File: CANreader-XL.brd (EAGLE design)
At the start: 66.7 x 61 mm, 73 parts, among them IC2 TJA1055T, IC3 BD9G101G, IC4 LM1117IMPX-3.3, IC5 STM32F107VBT, Q1 16MHz, U1 HC_05, U2 MCP2551, X1 MINI-USB, X2 SWD, X3 GPIO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

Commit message: Mount hole
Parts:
- moved LED1 0.51 mm to (3.17, 51.3), turned to 90 degrees
- moved LED3 0.25 mm to (3.17, 56.1)
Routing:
- net +3V3: track 361.5 -> 359.8 mm
- net GND: track 877.0 -> 875.7 mm
- net USB_VBUS: track 34.0 -> 35.2 mm
- net USB_D-: track 32.0 -> 33.2 mm
- net N$18: track 24.6 -> 23.4 mm
- net USB_D+: track 31.1 -> 32.1 mm
- net N$14: track 12.8 -> 13.4 mm

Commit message: Board name & version
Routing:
- net +3V3: track 359.8 -> 355.4 mm
- net PD7: track 55.6 -> 54.6 mm
- net PB10: track 16.1 -> 15.3 mm
- net PD4: track 61.4 -> 60.6 mm
- net PD3: track 73.3 -> 72.6 mm
- net RMII_MDC: track 48.1 -> 47.6 mm
- net RMII_REF_CLK: track 42.1 -> 41.6 mm
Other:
- board text added: "CANreader-XL"
- board text added: "https://github.com/autowp/CANreader-XL"
- board text added: "v0.1"

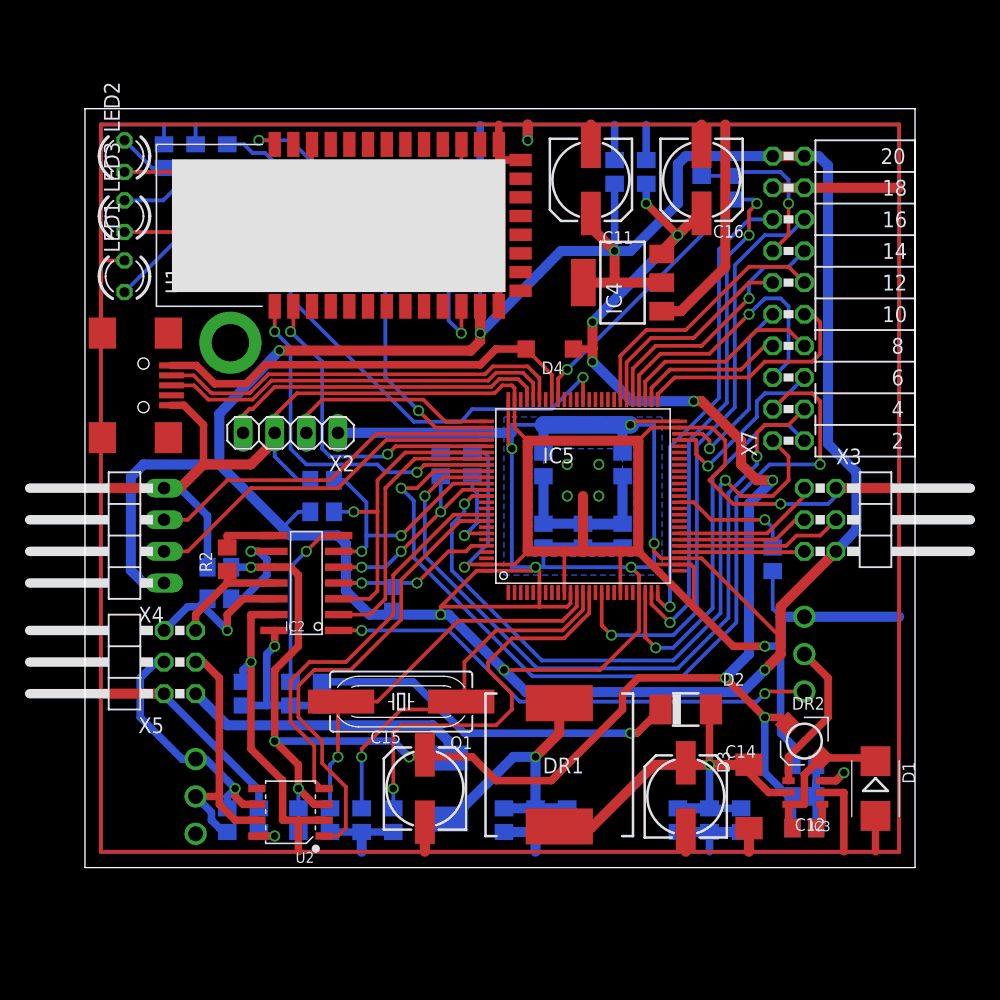
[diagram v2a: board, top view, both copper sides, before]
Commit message: Silk layers
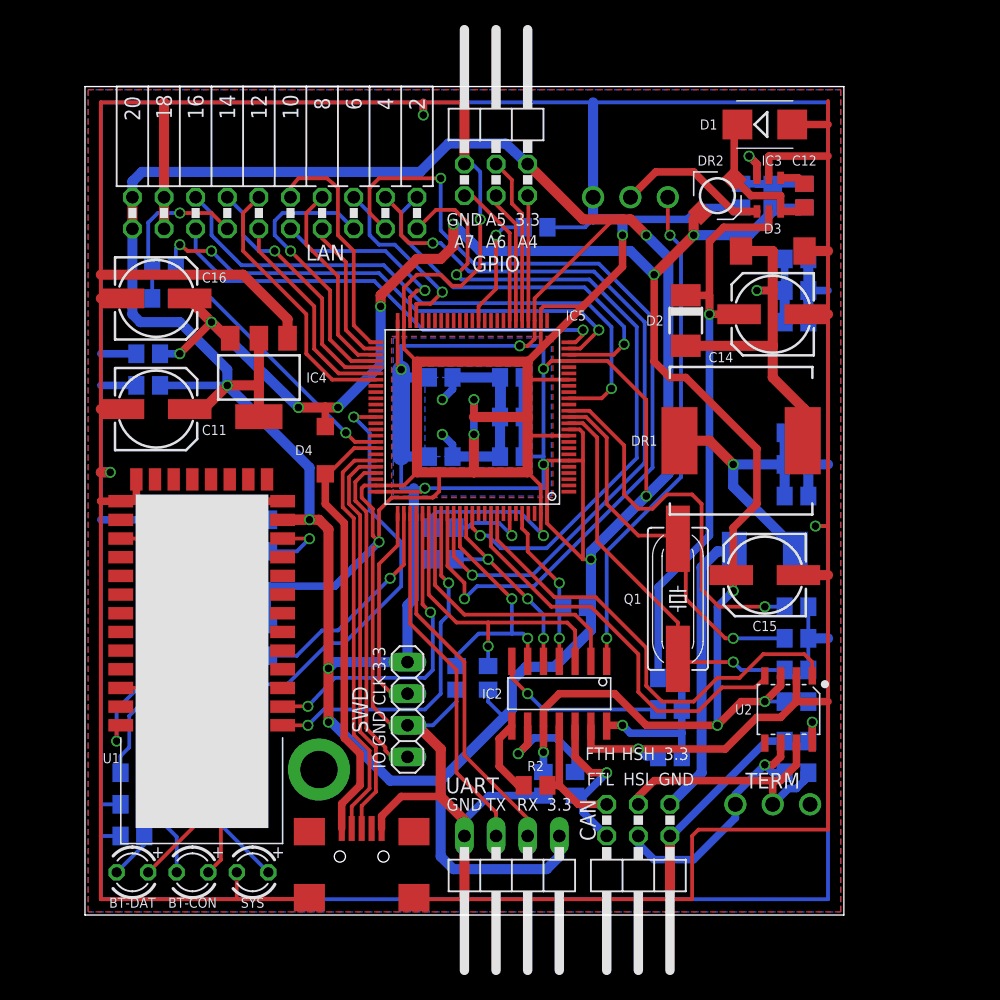
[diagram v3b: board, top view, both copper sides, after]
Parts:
- LED1: value USER -> SYS
- LED2: value HC-DATA -> BT-DAT
- LED3: value HC-CONN -> BT-CON
- moved LED2 57.5 mm to (3.81, 3.43), turned to 180 degrees
- moved R13 54.7 mm to (3.81, 6.35), turned to 180 degrees
- moved D1 54.1 mm to (54.6, 63.5), turned to 0 degrees
- moved LED3 53.0 mm to (8.64, 3.43), turned to 180 degrees
- moved R14 52.3 mm to (3.81, 8.89), turned to 180 degrees
- moved C12 50.8 mm to (57.8, 57.8), turned to 270 degrees
- moved C13 50.8 mm to (57.8, 57.8), turned to 270 degrees
- moved R21 50.1 mm to (3.81, 11.4), turned to 180 degrees
- moved LED1 49.0 mm to (13.5, 3.43), turned to 180 degrees
- moved R8 48.3 mm to (55.2, 57.8), turned to 90 degrees
- moved IC3 47.6 mm to (55.9, 56.5), turned to 180 degrees
- moved X8 46.4 mm to (55.2, 8.89), turned to 0 degrees
- moved R19 46.2 mm to (6.35, 52.1), turned to 0 degrees
- moved R7 46.0 mm to (52.7, 57.8), turned to 90 degrees
- moved R22 45.9 mm to (57.1, 11.4), turned to 180 degrees
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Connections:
- net BAT: now also C14.+, IC3.5
- net BAT1: no longer C14.+, IC3.5
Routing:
- net BAT: track 29.7 -> 49.1 mm
- net N$24: track 10.2 -> 5.85 mm
- net GND: track 875.7 -> 879.3 mm, vias 9 -> 12
- net HC_KEY: track 20.9 -> 18.0 mm
- net N$10: track 20.9 -> 22.8 mm
- net N$25: track 17.6 -> 19.3 mm
- net +3V3: track 355.4 -> 357.1 mm, vias 11 -> 12
- net N$7: track 4.71 -> 6.27 mm
- net +5V: track 148.8 -> 150.1 mm
- net NRST: track 32.4 -> 31.1 mm
- net N$6: track 46.7 -> 48.0 mm
- net N$8: track 8.30 -> 9.48 mm
- net BAT1: track 35.1 -> 34.4 mm
- net CAN1H: track 9.57 -> 10.2 mm
- net N$15: track 31.2 -> 31.7 mm
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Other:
- board size 66.7 x 61 mm -> 61 x 66.5 mm
- board text added: "+"
- board text added: "3.3"
- board text added: "A4"
- board text added: "A5"
- board text added: "A6"
- board text added: "A7"
- board text added: "CLK"
- board text added: "FTH"
- board text added: "FTL"
- board text added: "GND"
- board text added: "HSH"
- board text added: "HSL"
- board text added: "IO"
- board text added: "RX"
- board text added: "TX"

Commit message: VREF+, VREF-
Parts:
- removed X7: LAN, con-lsta:FE10-2W
- added R20, R24: 0, rcl:R0805
- added SW1: SLEEP, STM32_CAN-USB:SS12F27
- X6: value SLEEP -> LAN; device STM32_CAN-USB:SS12F27 -> con-lsta:FE10-2W
- moved X6 28.6 mm to (15.2, 56.4)
- renumbered X8 to SW2
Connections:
- net +3V3: now also R20.1, X6.19, X6.20; no longer X7.19, X7.20
- net EN: now also SW1.2; no longer X6.2
- net GND: now also R24.1, SW1.3, X6.17, X6.18; no longer X6.3, X7.17, X7.18
- net N$37: now also X6.13; no longer X7.13
- net PA0: now also X6.2; no longer X7.2
- net PB10: now also X6.6; no longer X7.6
- net PB14: now also X6.8; no longer X7.8
- net PB15: now also X6.5; no longer X7.5
- net PD3: now also X6.3; no longer X7.3
- net PD4: now also X6.4; no longer X7.4
- net PD7: now also X6.1; no longer X7.1
- net RMII_CRS_DV: now also X6.14; no longer X7.14
- net RMII_MDC: now also X6.16; no longer X7.16
- net RMII_MDIO: now also X6.15; no longer X7.15
- net RMII_RXD0: now also X6.11; no longer X7.11
- net RMII_RXD1: now also X6.12; no longer X7.12
- net RMII_TXD0: now also X6.10; no longer X7.10
- net RMII_TXD1: now also X6.7; no longer X7.7
- net RMII_TX_EN: now also X6.9; no longer X7.9
- net TJA_INH: now also SW1.1; no longer X6.1
- net VREF+: now also R20.2
- net VREF-: now also R24.2
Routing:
- net VREF-: track 0.00 -> 10.6 mm, vias 0 -> 1
- net GND: track 879.3 -> 889.0 mm, vias 12 -> 13
- net VREF+: track 0.00 -> 6.68 mm, vias 0 -> 1
- net +3V3: track 357.1 -> 361.5 mm, vias 12 -> 13

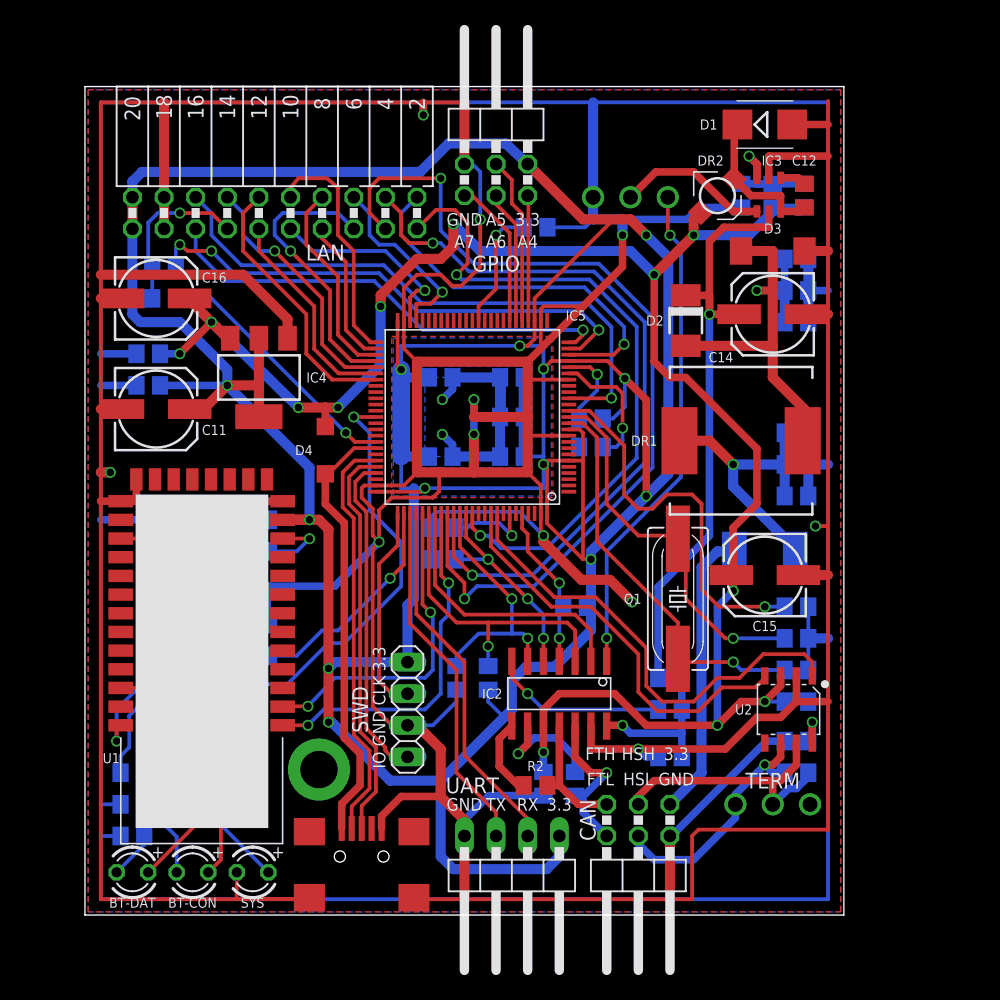
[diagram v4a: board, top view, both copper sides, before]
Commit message: Capacitors 0605 -> 0505
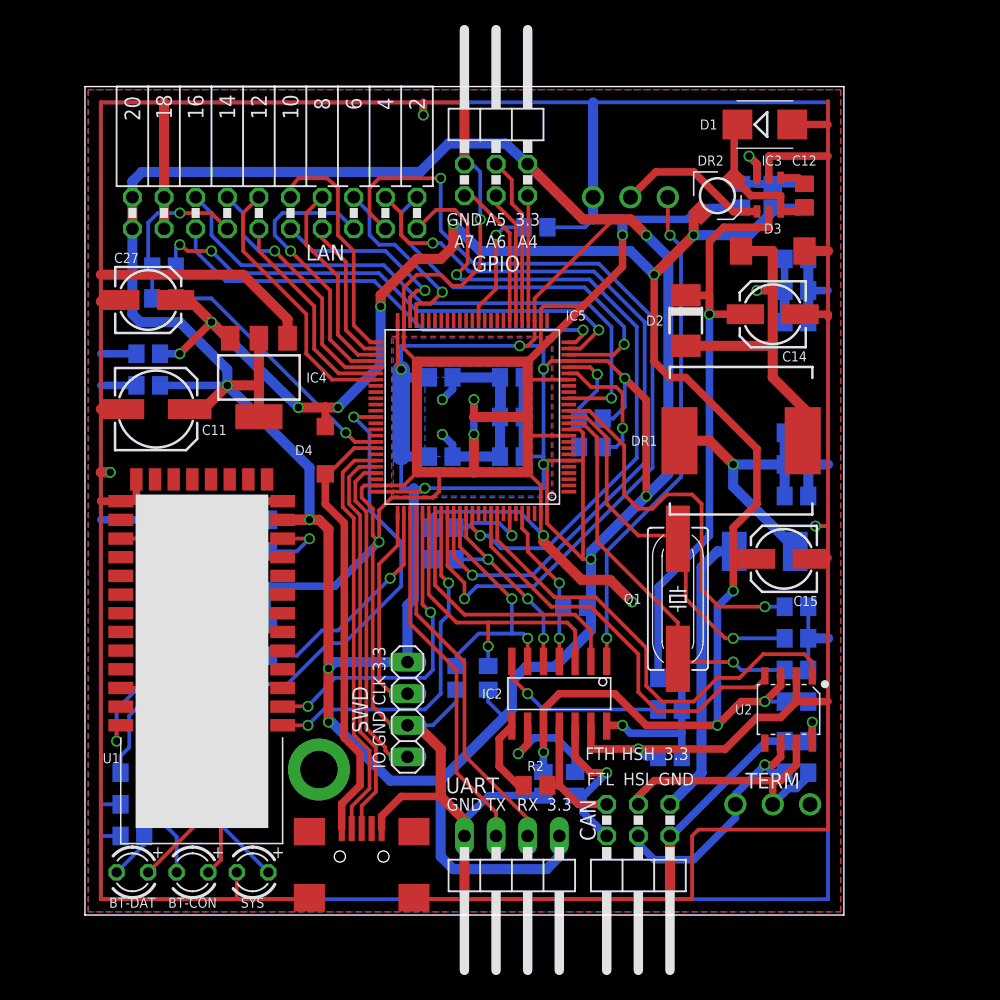
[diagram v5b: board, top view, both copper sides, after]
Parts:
- removed C16: 10uF, rcl:153CLV-0605
- added C27: 10uF/25v, rcl:153CLV-0505
- C14: device rcl:153CLV-0605 -> rcl:153CLV-0505
- C15: value 10uF -> 10uF/25v; device rcl:153CLV-0605 -> rcl:153CLV-0505
- moved C15 2.01 mm to (56.1, 28.6)
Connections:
- net +5V: now also C27.+; no longer C16.+
- net GND: now also C27.-; no longer C16.-
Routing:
- net +5V: track 150.1 -> 152.4 mm
- net BAT: track 49.1 -> 49.6 mm

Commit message: Capacitors improvements, HC RST to CPU
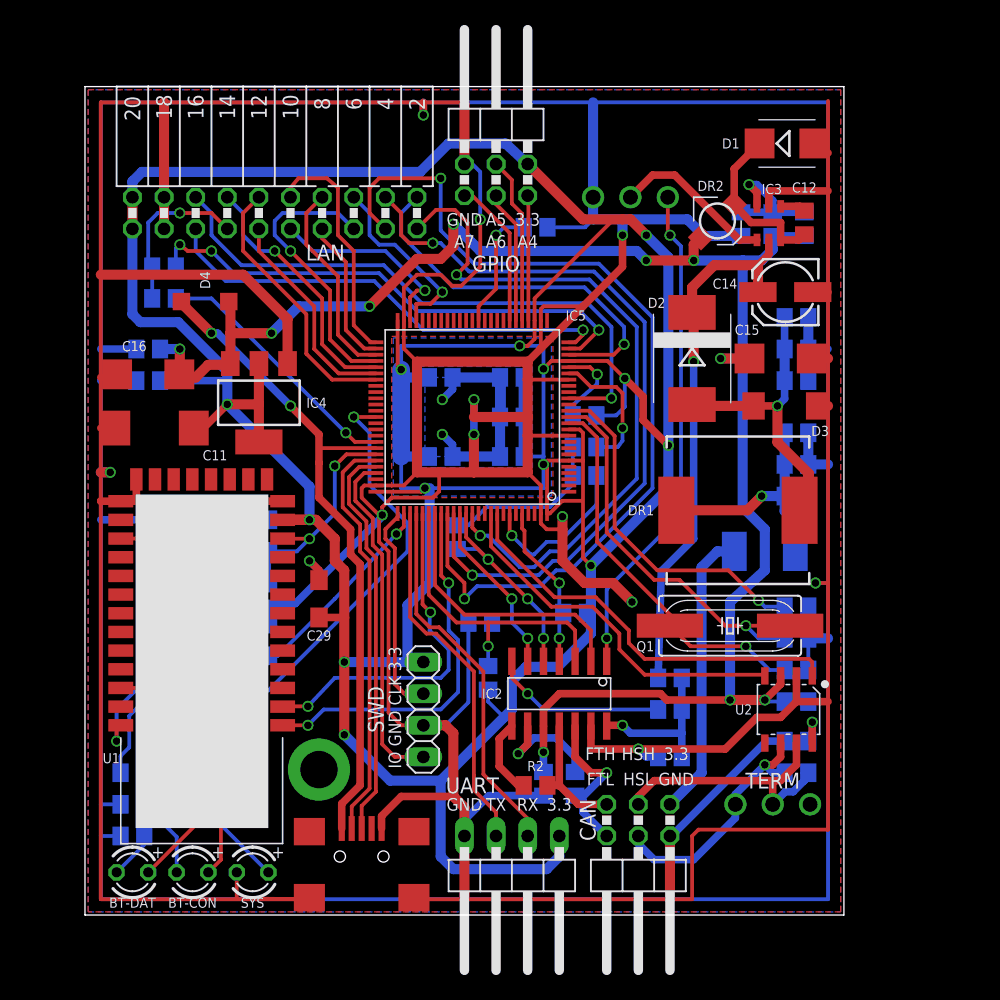
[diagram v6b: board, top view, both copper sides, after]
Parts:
- added C16: 10uF/25v, rcl:SMC_C
- added C29: 10uF/16v, rcl:SMC_A
- C11: device rcl:153CLV-0605 -> rcl:SMC_D
- C15: device rcl:153CLV-0505 -> rcl:SMC_C
- C27: value 10uF/25v -> 0.1; device rcl:153CLV-0505 -> rcl:C0805
- D2: value SK36A -> 3A/50V; device STM32_CAN-USB:DO-214AC -> diode:SMC
- moved C27 24.4 mm to (13.8, 26.7), flipped to the bottom
- moved C15 16.1 mm to (55.9, 44.7), turned to 0 degrees
- moved D4 15.4 mm to (9.65, 49.3), turned to 180 degrees
- moved D3 12.5 mm to (56.3, 40.9)
- moved R9 12.1 mm to (40.1, 35.3)
- moved DR1 5.59 mm to (52.5, 32.5)
- moved R12 4.84 mm to (31.8, 23.5), turned to 180 degrees
- moved Q1 4.71 mm to (51.8, 23.2), turned to 180 degrees
- moved C22 4.70 mm to (57.1, 42.9)
- moved C23 4.70 mm to (57.1, 48.0)
- moved C24 4.70 mm to (57.1, 45.5)
- moved D2 3.09 mm to (48.8, 44.7)
- moved D1 2.34 mm to (56.4, 62.0)
- moved IC3 2.29 mm to (55.9, 54.2)
- moved C13 2.29 mm to (57.8, 55.5)
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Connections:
- removed net N$24: R17.2, U1.11
- new net HC_RESET: C27.1, IC5.69, R17.2, U1.11
- net +3V3: now also C29.+
- net +5V: now also C16.+; no longer C27.+
- net GND: now also C16.-, C27.2, C29.-; no longer C27.-
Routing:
- net USB_VBUS: track 35.5 -> 54.9 mm, vias 0 -> 2
- net HC_RESET: track 0.00 -> 18.8 mm, vias 0 -> 2
- net +5V: track 152.4 -> 138.4 mm, vias 12 -> 10
- net GND: track 888.6 -> 899.2 mm, vias 13 -> 14
- net BAT1: track 34.4 -> 26.4 mm
- net BAT: track 49.6 -> 43.1 mm
- net N$3: track 6.94 -> 13.3 mm
- net N$24: track 5.85 -> 0.00 mm, vias 1 -> 0
- net TJA_EN: track 20.7 -> 15.7 mm
- net CAN2_TX: track 37.5 -> 33.2 mm
- net N$18: track 23.4 -> 19.3 mm
- net N$2: track 30.1 -> 33.5 mm
- net CAN2_RX: track 33.2 -> 29.9 mm
- net NRST: track 31.1 -> 28.2 mm
- net +3V3: track 361.5 -> 358.8 mm
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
